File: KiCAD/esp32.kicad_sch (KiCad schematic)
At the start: 13 parts, among them J1 Edge2x6_Connector, J2 USB_B_Micro, U1 ESP32-WROOM-32, U2 AMS1117-3.3

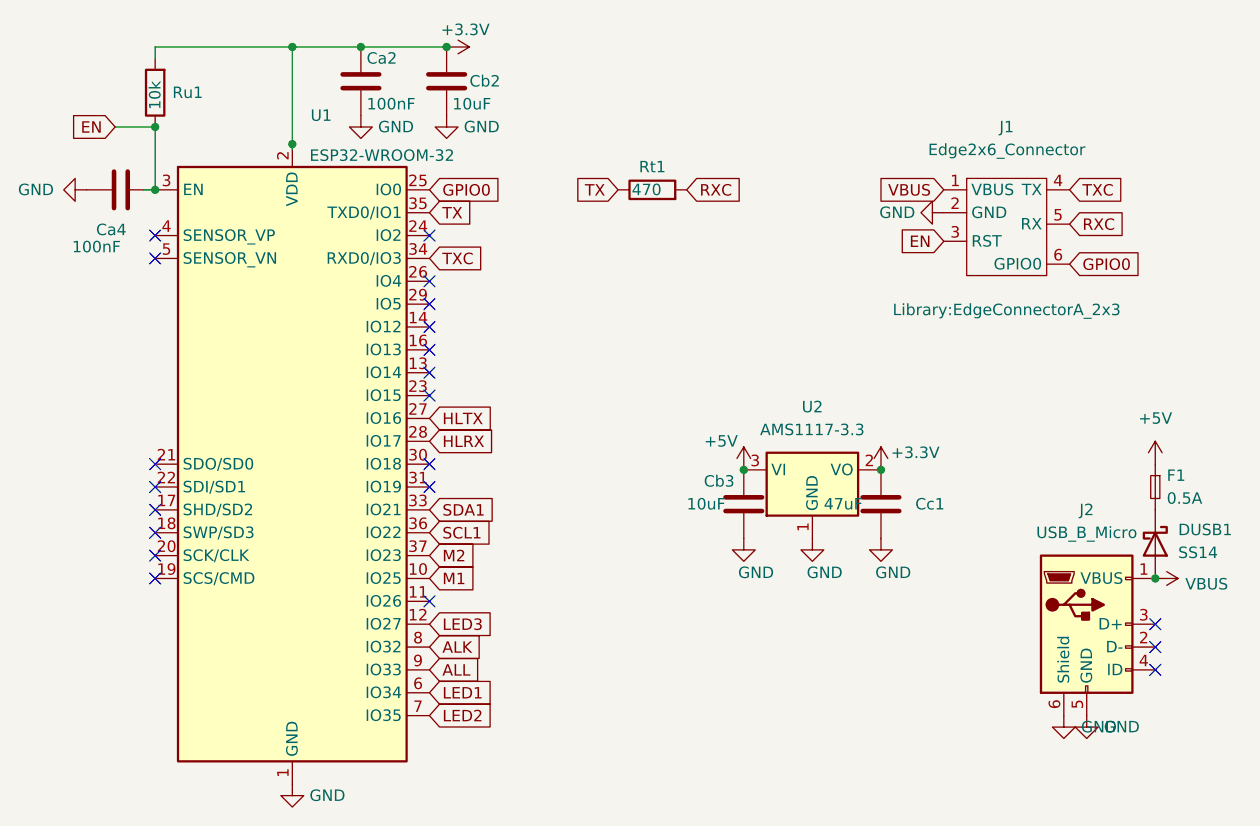
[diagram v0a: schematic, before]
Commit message: Updates for v10 Room133 board (#13)
- Update KiCad design
- SHTC3 has better thermal isolation.  Ebox updated for its new position.
- Fixed library for edge footprint
- Two LEDs were driven using input-only pins (gpio34,gpio35), so moved to gpio18, gpio19.
- Updated to KiCAD 8.0 format
- Documentation for PIR wire.
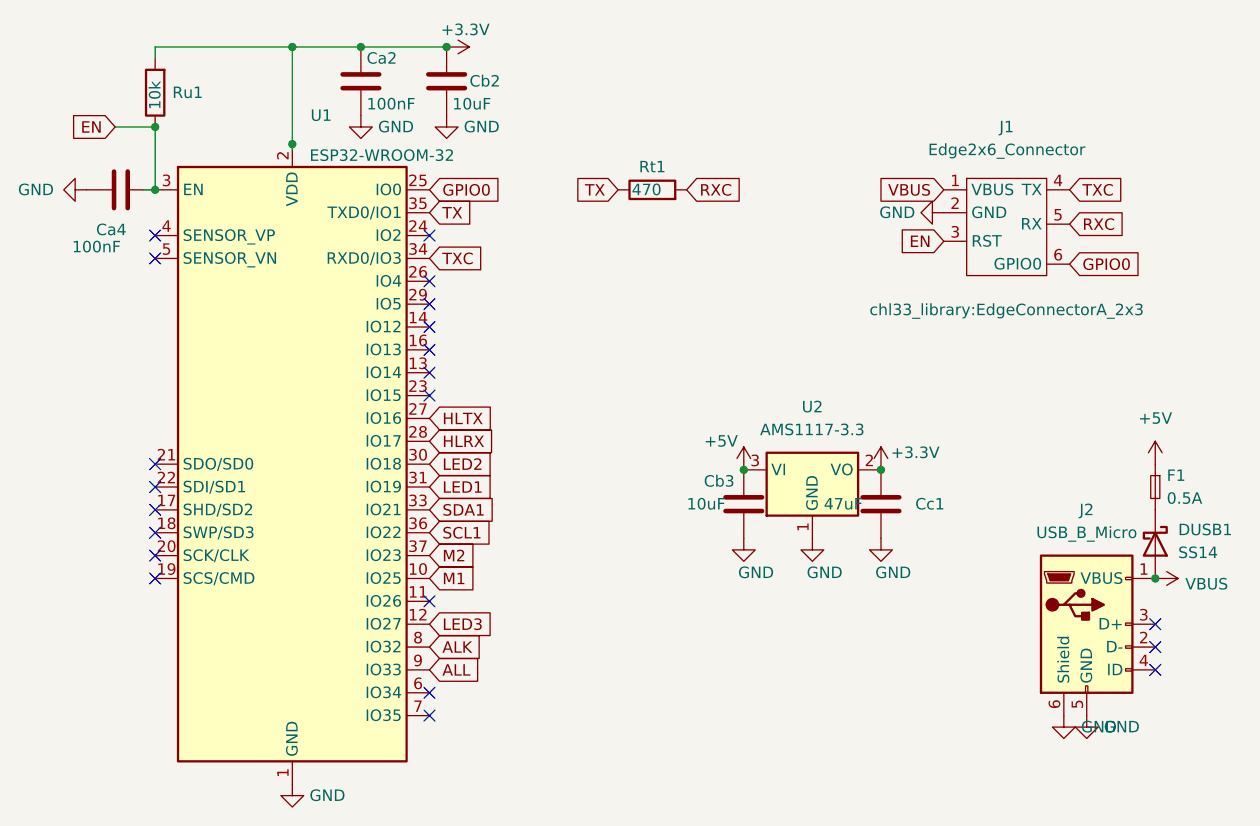
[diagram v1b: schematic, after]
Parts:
- J1: footprint Library:EdgeConnectorA_2x3 -> chl33_library:EdgeConnectorA_2x3
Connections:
- net LED1: now also U1.31 (IO19); no longer U1.6 (IO34)
- net LED2: now also U1.30 (IO18); no longer U1.7 (IO35)
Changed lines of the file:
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@@
 	)
 	(no_connect
-		(at 66.04 76.2)
+		(at 66.04 101.6)
 	)
 	(no_connect
@@
 	)
 	(no_connect
-		(at 66.04 73.66)
+		(at 66.04 99.06)
 	)
 	(no_connect
@@
 	(global_label "LED2"
 		(shape input)
-		(at 66.04 101.6 0)
-		(fields_autoplaced yes)
-		(effects
-			(font
-				(size 1.27 1.27)
-			)
-			(justify left)
-		)
-		(property "Intersheetrefs" "${INTERSHEET_REFS}"
-			(at 73.6818 101.6 0)
+		(at 66.04 73.66 0)
+		(fields_autoplaced yes)
+		(effects
+			(font
+				(size 1.27 1.27)
+			)
+			(justify left)
+		)
+		(property "Intersheetrefs" "${INTERSHEET_REFS}"
+			(at 73.6818 73.66 0)
 			(effects
 				(font
@@
 	(global_label "LED1"
 		(shape input)
-		(at 66.04 99.06 0)
-		(fields_autoplaced yes)
-		(effects
-			(font
-				(size 1.27 1.27)
-			)
-			(justify left)
-		)
-		(property "Intersheetrefs" "${INTERSHEET_REFS}"
-			(at 73.6818 99.06 0)
+		(at 66.04 76.2 0)
+		(fields_autoplaced yes)
+		(effects
+			(font
+				(size 1.27 1.27)
+			)
+			(justify left)
+		)
+		(property "Intersheetrefs" "${INTERSHEET_REFS}"
+			(at 73.6818 76.2 0)
 			(effects
 				(font
@@
 			)
 		)
-		(property "Footprint" "Library:EdgeConnectorA_2x3"
+		(property "Footprint" "chl33_library:EdgeConnectorA_2x3"
 			(at 130.175 56.515 0)
 			(effects
